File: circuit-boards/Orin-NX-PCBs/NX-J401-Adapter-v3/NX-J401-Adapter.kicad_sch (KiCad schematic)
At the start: 13 parts, among them J1 Power, J2 CAN-NX, J3 NX-BUTTON, J4 CONSOLE, J5 18V_OUT, J6 CAN-NX, J7 CAN-NX

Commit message: NX Adapter interim checking
Signed-off-by: Scott <sgberman1@gmail.com>
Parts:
- removed J4: CONSOLE, NX-J401-Adapter:70555-0005, symbol Connector:Conn_01x06_Pin
- added J12: CONSOLE, NX-J401-Adapter:70555-0002, symbol Connector:Conn_01x03_Pin
- added SW1: RESET, NX-J401-Adapter:SW_TL1105VF100Q_EWI, symbol Switch:SW_Push
- added SW2: RECOVERY, NX-J401-Adapter:SW_TL1105VF100Q_EWI, symbol Switch:SW_Push
- R17: value 4.99k-1%-0603 -> 4.99k-1%-0805; footprint Resistor_SMD:R_0603_1608Metric -> Resistor_SMD:R_0805_2012Metric; DIST Digikey -> (none); DIST P/N 311-4.99KHRCT-ND -> (none); MFG Yageo -> (none); MFG P/N RC0603FR-074K99L -> (none)
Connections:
- net RTN: now also J12.1 (Pin_1), SW1.2, SW2.2
- net UART2_RXD: now also J12.2 (Pin_2)
- net UART2_TXD: now also J12.3 (Pin_3)
- net ~{REC}: now also SW2.1
- net ~{SYS_RESET}: now also SW1.1

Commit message: interim checkin of NX Adapter board
Signed-off-by: Scott Berman <scott.berman@bluerivertech.com>
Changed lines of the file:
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@@
+	)
+	(junction
+		(at 207.01 217.17)
+		(diameter 0)
+		(color 0 0 0 0)
 	)
 	(junction
@@
 	)
 	(junction
+		(at 207.01 207.01)
+		(diameter 0)
+		(color 0 0 0 0)
+	)
+	(junction
 		(at 165.1 77.47)
 		(diameter 0)
@@
 	(wire
 		(pts
+			(xy 207.01 207.01) (xy 207.01 217.17)
+		)
+		(stroke
+			(width 0)
+			(type default)
+		)
+	)
+	(wire
+		(pts
 			(xy 193.04 209.55) (xy 224.79 209.55)
 		)
@@
 	(wire
 		(pts
+			(xy 207.01 207.01) (xy 224.79 207.01)
+		)
+		(stroke
+			(width 0)
+			(type default)
+		)
+	)
+	(wire
+		(pts
 			(xy 193.04 214.63) (xy 245.11 214.63)
 		)
@@
 	(wire
 		(pts
-			(xy 193.04 207.01) (xy 224.79 207.01)
-		)
-		(stroke
+			(xy 193.04 207.01) (xy 207.01 207.01)
+		)
+		(stroke

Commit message: Check in of NX Adapter and Indicator boards.  Complete pending review
Signed-off-by: Scott <sgberman1@gmail.com>
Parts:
- R17: DIST (none) -> Digikey; DIST P/N (none) -> 311-499CRCT-ND; MFG (none) -> Yageo; MFG P/N (none) -> RC0805FR-07499RL
- renumbered H4 to H2, H2 to H3, H3 to H4, J2 to J10, J3 to J11, J5 to J4, J1 to J6, J6 to J8, J12 to J9
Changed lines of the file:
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@@
 		(dnp no)
 		(fields_autoplaced yes)
-		(property "Reference" "H4"
+		(property "Reference" "H2"
 			(at 156.21 252.73 0)
 			(effects
@@
 			(project "NX-J401-Adapter"
 				(path "/cc31ce4b-09ab-4aea-a1d3-ed84696ba658"
-					(reference "H4")
+					(reference "H2")
 					(unit 1)
 				)
@@
 			)
 		)
-		(property "Datasheet" "~"
+		(property "Datasheet" "Components/YageoPYu-RC_Group_51_RoHS_L_12.pdf"
 			(at 165.1 71.12 0)
 			(effects
@@
 			)
 		)
-		(property "MFG" ""
+		(property "MFG" "Yageo"
 			(at 165.1 71.12 0)
 			(effects
@@
 			)
 		)
-		(property "MFG P/N" ""
+		(property "MFG P/N" "RC0805FR-07499RL"
 			(at 165.1 71.12 0)
 			(effects
@@
 			)
 		)
-		(property "DIST" ""
+		(property "DIST" "Digikey"
 			(at 165.1 71.12 0)
 			(effects
@@
 			)
 		)
-		(property "DIST P/N" ""
+		(property "DIST P/N" "311-499CRCT-ND"
 			(at 165.1 71.12 0)
 			(effects
@@
 		(dnp no)
 		(fields_autoplaced yes)
-		(property "Reference" "J3"
+		(property "Reference" "J11"
 			(at 188.595 201.93 0)
 			(effects
@@
 			)
 		)
-		(property "Datasheet" "Components/Molex-70543-0001.pdf"
+		(property "Datasheet" "Components/Molex-705430001_sd.pdf"
 			(at 187.96 212.09 0)
 			(effects
@@
 			(project ""
 				(path "/cc31ce4b-09ab-4aea-a1d3-ed84696ba658"
-					(reference "J3")
+					(reference "J11")
 					(unit 1)
 				)
@@
 		(dnp no)
 		(fields_autoplaced yes)
-		(property "Reference" "H3"
+		(property "Reference" "H4"
 			(at 156.21 246.38 0)
 			(effects
@@
 			(project "NX-J401-Adapter"
 				(path "/cc31ce4b-09ab-4aea-a1d3-ed84696ba658"
-					(reference "H3")
+					(reference "H4")
 					(unit 1)
 				)
@@
 		(dnp no)
 		(fields_autoplaced yes)
-		(property "Reference" "H2"
+		(property "Reference" "H3"
 			(at 137.16 252.73 0)
 			(effects
@@
 			(project "NX-J401-Adapter"
 				(path "/cc31ce4b-09ab-4aea-a1d3-ed84696ba658"
-					(reference "H2")
+					(reference "H3")
 					(unit 1)
 				)
@@
 		(on_board yes)
 		(dnp no)
-		(property "Reference" "J6"
+		(property "Reference" "J8"
 			(at 292.1 156.21 0)
 			(effects
@@
 			(project "NX-J401-Adapter"
 				(path "/cc31ce4b-09ab-4aea-a1d3-ed84696ba658"
-					(reference "J6")
+					(reference "J8")
 					(unit 1)
 				)
@@
 		(dnp no)
 		(fields_autoplaced yes)
-		(property "Reference" "J12"
+		(property "Reference" "J9"
 			(at 231.14 208.2799 0)
 			(effects
@@
 			)
 		)
-		(property "Datasheet" "Components/Molex-70543-0001.pdf"
+		(property "Datasheet" "Components/Molex-70555-0001.pdf"
 			(at 229.87 209.55 0)
 			(effects
@@
 			(project ""
 				(path "/cc31ce4b-09ab-4aea-a1d3-ed84696ba658"
-					(reference "J12")
+					(reference "J9")
 					(unit 1)
 				)
@@
 		(dnp no)
 		(fields_autoplaced yes)
-		(property "Reference" "J1"
+		(property "Reference" "J6"
 			(at 146.685 53.34 0)
 			(effects
@@
 			(project "NX-J401-Adapter"
 				(path "/cc31ce4b-09ab-4aea-a1d3-ed84696ba658"
-					(reference "J1")
+					(reference "J6")
 					(unit 1)
 				)
@@
 		(on_board yes)
 		(dnp no)
-		(property "Reference" "J5"
+		(property "Reference" "J4"
 			(at 267.335 53.34 0)
 			(effects
@@
 			(project "NX-J401-Adapter"
 				(path "/cc31ce4b-09ab-4aea-a1d3-ed84696ba658"
-					(reference "J5")
+					(reference "J4")
 					(unit 1)
 				)
@@
 			)
 		)
-		(property "Datasheet" "https://files.seeedstudio.com/wiki/J401/reComputer_J401_SCH_V1.0.pdf"
+		(property "Datasheet" "Components/SeeedStudio-reComputer_J401_SCH_V1.0.pdf"
 			(at 288.29 93.98 0)
 			(effects
@@
 		(on_board yes)
 		(dnp no)
-		(property "Reference" "J2"
+		(property "Reference" "J10"
 			(at 158.75 156.2099 0)
 			(effects
@@
 			(project "NX-J401-Adapter"
 				(path "/cc31ce4b-09ab-4aea-a1d3-ed84696ba658"
-					(reference "J2")
-					(unit 1)
-				)
+					(reference "J10")
+					(unit 1)
+				)

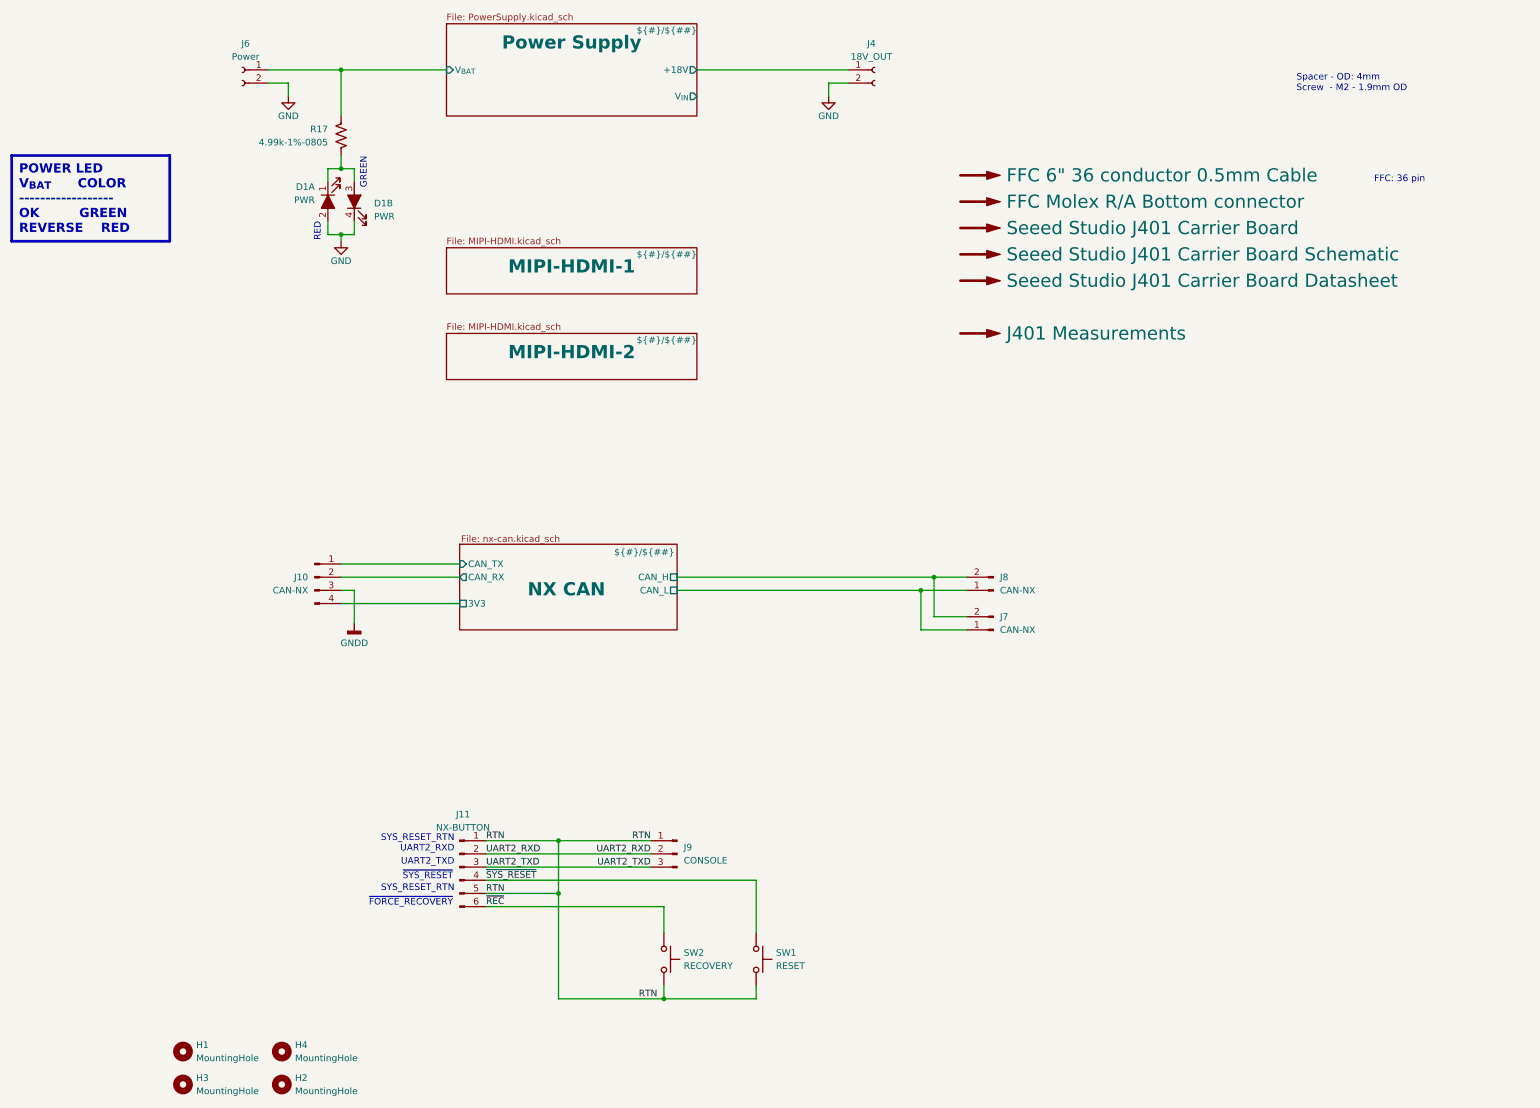
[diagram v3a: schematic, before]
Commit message: Minor update to NX-J401-Adapter-v3
Signed-off-by: Scott Berman <scott.berman@bluerivertech.com>
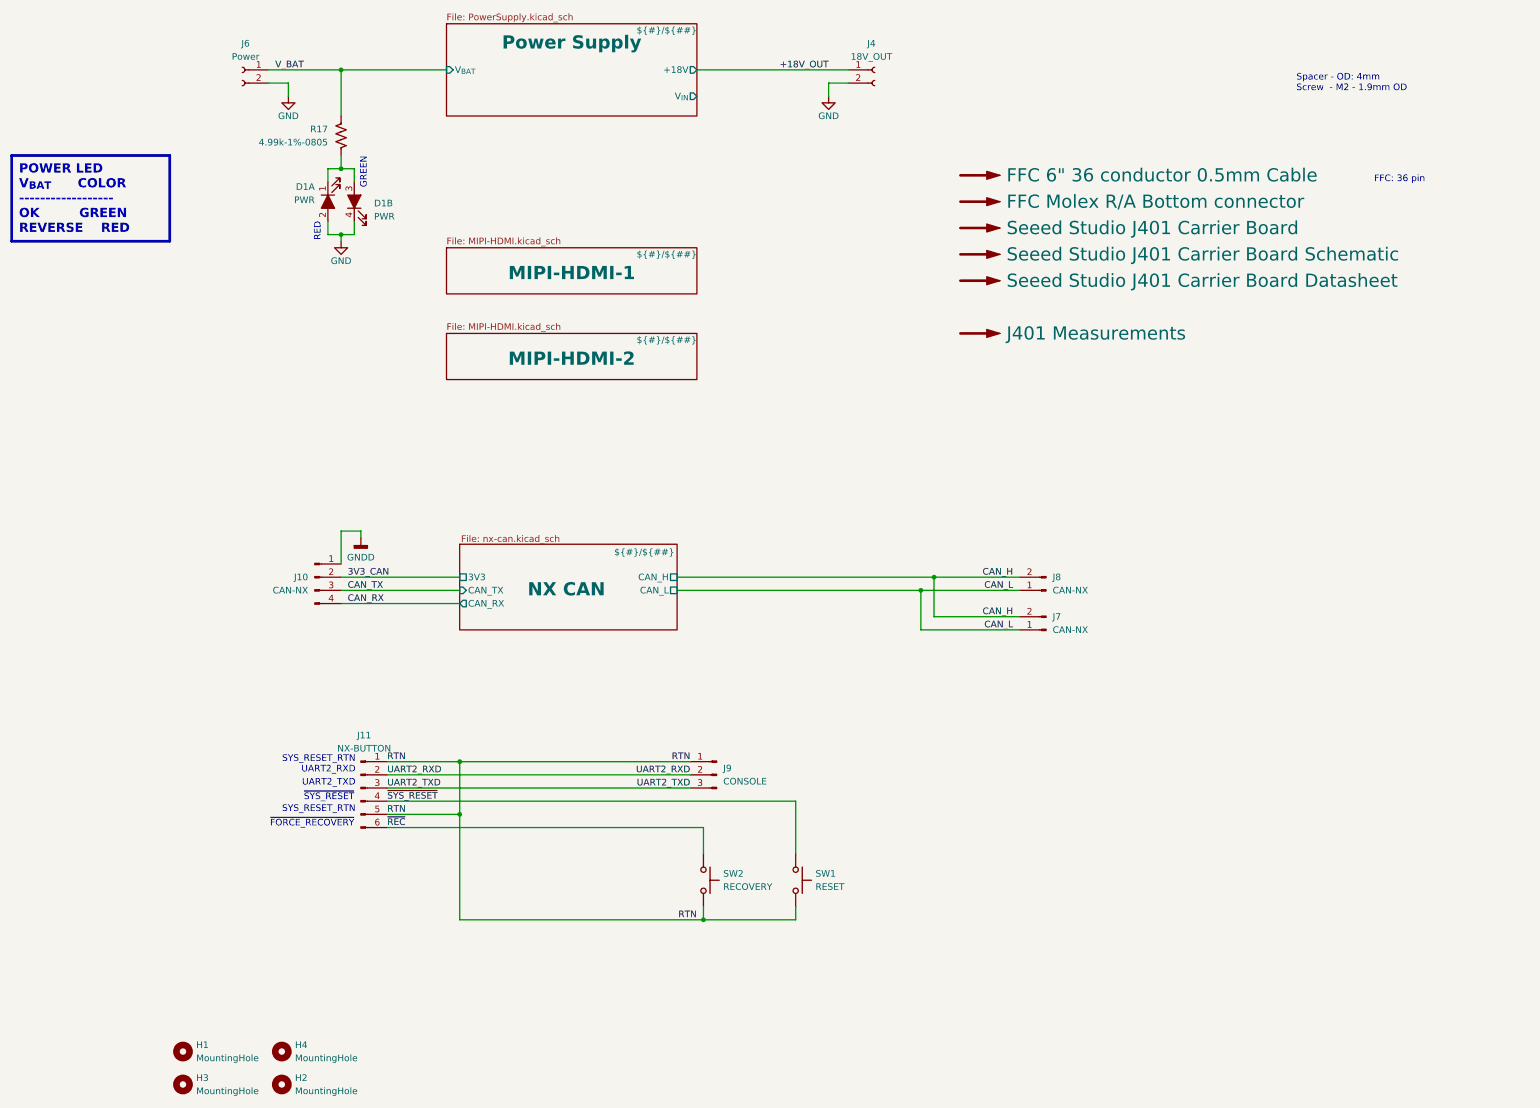
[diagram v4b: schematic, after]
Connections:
- net NX CAN/CAN_TX is gone; now on net GNDD: J10.1 (Pin_1)
- net GNDD: no longer J10.3 (Pin_3)
- net NX CAN/3V3 renamed CAN_RX
- net NX CAN/CAN_H renamed CAN_H
- net NX CAN/CAN_L renamed CAN_L
- net NX CAN/CAN_RX renamed 3V3_CAN
- net Power Supply/+18V renamed +18V_OUT
- net Power Supply/V_{BAT} renamed V_BAT
- new net CAN_TX: J10.3 (Pin_3)
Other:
- moved on the sheet: J11, J7, J8, J9, SW1, SW2

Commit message: Updated diff pairs and power supply layout
Signed-off-by: Scott <sgberman1@gmail.com>
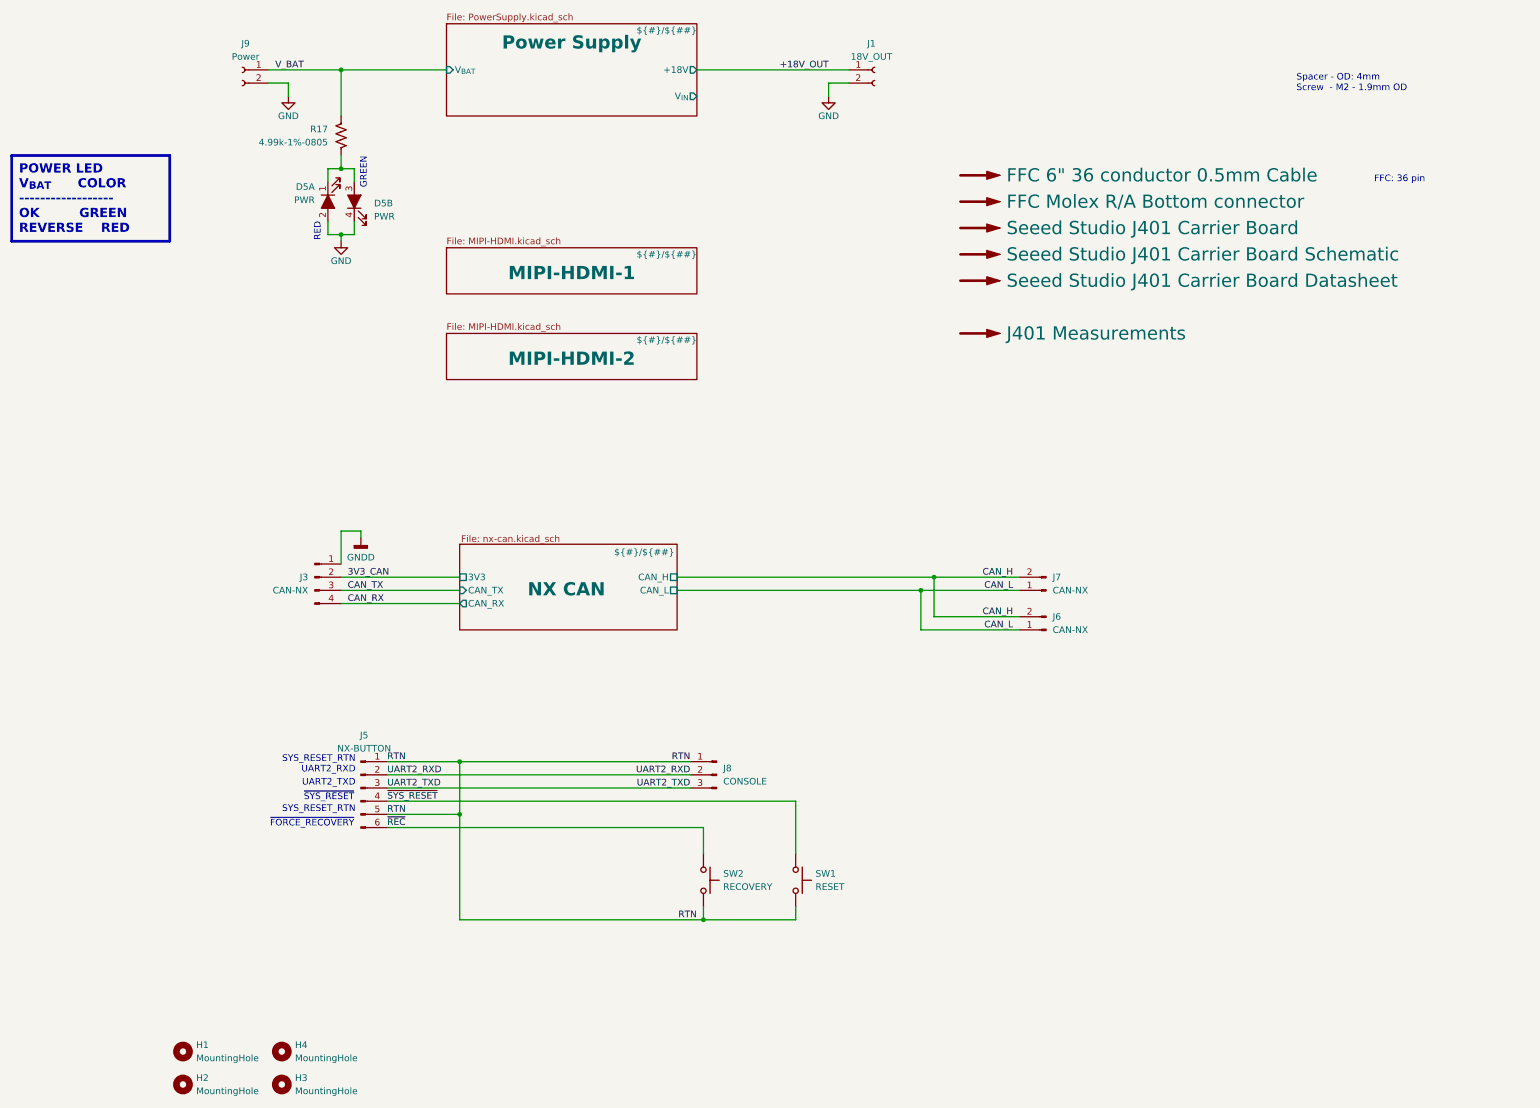
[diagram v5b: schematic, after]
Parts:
- renumbered D1 to D5, H3 to H2, H2 to H3, J4 to J1, J10 to J3, J11 to J5, J7 to J6, J8 to J7, J9 to J8, J6 to J9
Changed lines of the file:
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@@
 	(title_block
 		(title "NX J401 Adapter")
-		(date "2024-08-05")
+		(date "2024-08-10")
 		(rev "3")
 		(company "971 Spartan Robotics")
@@
 		(dnp no)
 		(fields_autoplaced yes)
-		(property "Reference" "H2"
+		(property "Reference" "H3"
 			(at 156.21 252.73 0)
 			(effects
@@
 			(project "NX-J401-Adapter"
 				(path "/cc31ce4b-09ab-4aea-a1d3-ed84696ba658"
-					(reference "H2")
+					(reference "H3")
 					(unit 1)
 				)
@@
 		(dnp no)
 		(fields_autoplaced yes)
-		(property "Reference" "D1"
+		(property "Reference" "D5"
 			(at 171.45 84.1375 90)
 			(effects
@@
 			(project "NX-J401-Adapter"
 				(path "/cc31ce4b-09ab-4aea-a1d3-ed84696ba658"
-					(reference "D1")
+					(reference "D5")
 					(unit 2)
 				)
@@
 			(project "NX-J401-Adapter"
 				(path "/cc31ce4b-09ab-4aea-a1d3-ed84696ba658"
-					(reference "R1")
+					(reference "R9")
 					(unit 1)
 				)
@@
 		(dnp no)
 		(fields_autoplaced yes)
-		(property "Reference" "J11"
+		(property "Reference" "J5"
 			(at 169.545 186.69 0)
 			(effects
@@
 			(project ""
 				(path "/cc31ce4b-09ab-4aea-a1d3-ed84696ba658"
-					(reference "J11")
+					(reference "J5")
 					(unit 1)
 				)
@@
 		(on_board yes)
 		(dnp no)
-		(property "Reference" "D1"
+		(property "Reference" "D5"
 			(at 160.02 80.9625 90)
 			(effects
@@
 			(project "NX-J401-Adapter"
 				(path "/cc31ce4b-09ab-4aea-a1d3-ed84696ba658"
-					(reference "D1")
+					(reference "D5")
 					(unit 1)
 				)
@@
 		(on_board yes)
 		(dnp no)
-		(property "Reference" "J7"
+		(property "Reference" "J6"
 			(at 302.26 163.83 0)
 			(effects
@@
 			(project "NX-J401-Adapter"
 				(path "/cc31ce4b-09ab-4aea-a1d3-ed84696ba658"
-					(reference "J7")
+					(reference "J6")
 					(unit 1)
 				)
@@
 		(dnp no)
 		(fields_autoplaced yes)
-		(property "Reference" "H3"
+		(property "Reference" "H2"
 			(at 137.16 252.73 0)
 			(effects
@@
 			(project "NX-J401-Adapter"
 				(path "/cc31ce4b-09ab-4aea-a1d3-ed84696ba658"
-					(reference "H3")
+					(reference "H2")
 					(unit 1)
 				)
@@
 		(on_board yes)
 		(dnp no)
-		(property "Reference" "J8"
+		(property "Reference" "J7"
 			(at 302.26 156.21 0)
 			(effects
@@
 			(project "NX-J401-Adapter"
 				(path "/cc31ce4b-09ab-4aea-a1d3-ed84696ba658"
-					(reference "J8")
+					(reference "J7")
 					(unit 1)
 				)
@@
 		(dnp no)
 		(fields_autoplaced yes)
-		(property "Reference" "J9"
+		(property "Reference" "J8"
 			(at 238.76 193.0399 0)
 			(effects
@@
 			(project ""
 				(path "/cc31ce4b-09ab-4aea-a1d3-ed84696ba658"
-					(reference "J9")
+					(reference "J8")
 					(unit 1)
 				)
@@
 		(dnp no)
 		(fields_autoplaced yes)
-		(property "Reference" "J6"
+		(property "Reference" "J9"
 			(at 146.685 53.34 0)
 			(effects
@@
 			(project "NX-J401-Adapter"
 				(path "/cc31ce4b-09ab-4aea-a1d3-ed84696ba658"
-					(reference "J6")
+					(reference "J9")
 					(unit 1)
 				)
@@
 		(on_board yes)
 		(dnp no)
-		(property "Reference" "J4"
+		(property "Reference" "J1"
 			(at 267.335 53.34 0)
 			(effects
@@
 			(project "NX-J401-Adapter"
 				(path "/cc31ce4b-09ab-4aea-a1d3-ed84696ba658"
-					(reference "J4")
+					(reference "J1")
 					(unit 1)
 				)
@@
 		(on_board yes)
 		(dnp no)
-		(property "Reference" "J10"
+		(property "Reference" "J3"
 			(at 158.75 156.2099 0)
 			(effects
@@
 			(project "NX-J401-Adapter"
 				(path "/cc31ce4b-09ab-4aea-a1d3-ed84696ba658"
-					(reference "J10")
+					(reference "J3")
 					(unit 1)
 				)
